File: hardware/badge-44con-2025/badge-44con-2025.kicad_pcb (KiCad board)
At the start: 2 copper layers, 100 x 100 mm, 28 parts, among them J1 128x64 OLED Display, J2 Conn_02x03_Odd_Even, SW1 RESET, SW2 SW_Nidec_CAS-120A1, U1 ESP32-WEMOS D1 mini, U2 CH32V003FxPx, U3 MT3608_Boost_converter, U4 AD8317_Module

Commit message: feat(Hw):Added_labels_and_changed_switch
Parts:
- added kibuzzard-68957673: G***, kibuzzard-68957673, B.Cu at (123.2, 124.5)
- added kibuzzard-689576B7: G***, kibuzzard-689576B7, B.Cu at (123.7, 107.6)
- added kibuzzard-689576CB: G***, kibuzzard-689576CB, B.Cu at (125.8, 48.4)
- added kibuzzard-689576F4: G***, kibuzzard-689576F4, B.Cu at (197.0, 68.4)
- added kibuzzard-689576FF: G***, kibuzzard-689576FF, B.Cu at (197.1, 70.5)
- added kibuzzard-68957745: G***, kibuzzard-68957745, B.Cu at (201.4, 77.7)
- added kibuzzard-6895776E: G***, kibuzzard-6895776E, B.Cu at (200.8, 78.6)
- added kibuzzard-68957B6E: G***, kibuzzard-68957B6E, B.Cu at (143.1, 132.1)
- added kibuzzard-68957F6B: G***, kibuzzard-68957F6B, B.Cu at (115.5, 118.0)
- JP2, JP3: footprint Jumper:SolderJumper-3_P1.3mm_Open_RoundedPad1.0x1.5mm -> Jumper:SolderJumper-3_P1.3mm_Bridged2Bar12_RoundedPad1.0x1.5mm
- SW2: footprint badge-44con-2025:a12013100ux0116 -> badge-44con-2025:JS102011SAQN; moved to B.Cu
- moved JP2 9.05 mm to (155.9, 63.0), turned to 0 degrees
- moved JP3 1.40 mm to (153.1, 55.7)
- moved SW2 1.07 mm to (110.8, 118.0)
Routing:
- net /CH3_SDA: track 22.2 -> 8.92 mm
- net /SDA_ESP: track 58.6 -> 54.1 mm, vias 1 -> 2
- net +5V: track 84.4 -> 88.2 mm, vias 0 -> 3
- net /CH3_SCL: track 19.2 -> 17.8 mm
- net /SCL: track 5.15 -> 3.89 mm
- net +5VP: track 77.1 -> 76.0 mm
- net /SCL_ESP: track 46.2 -> 45.2 mm
- net GND: vias 6 -> 33
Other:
- outline, holes or cut-outs redrawn

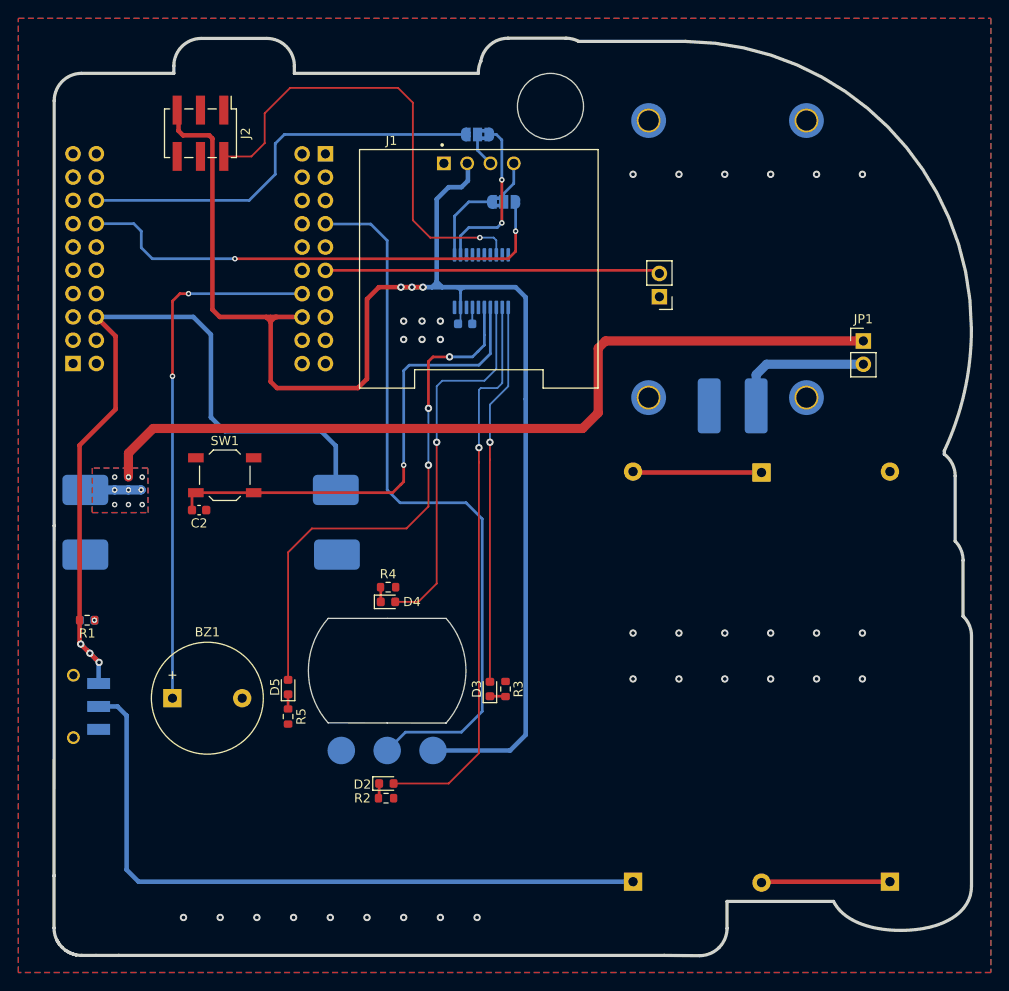
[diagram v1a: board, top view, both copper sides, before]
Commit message: feat(Hw):Added_buttons
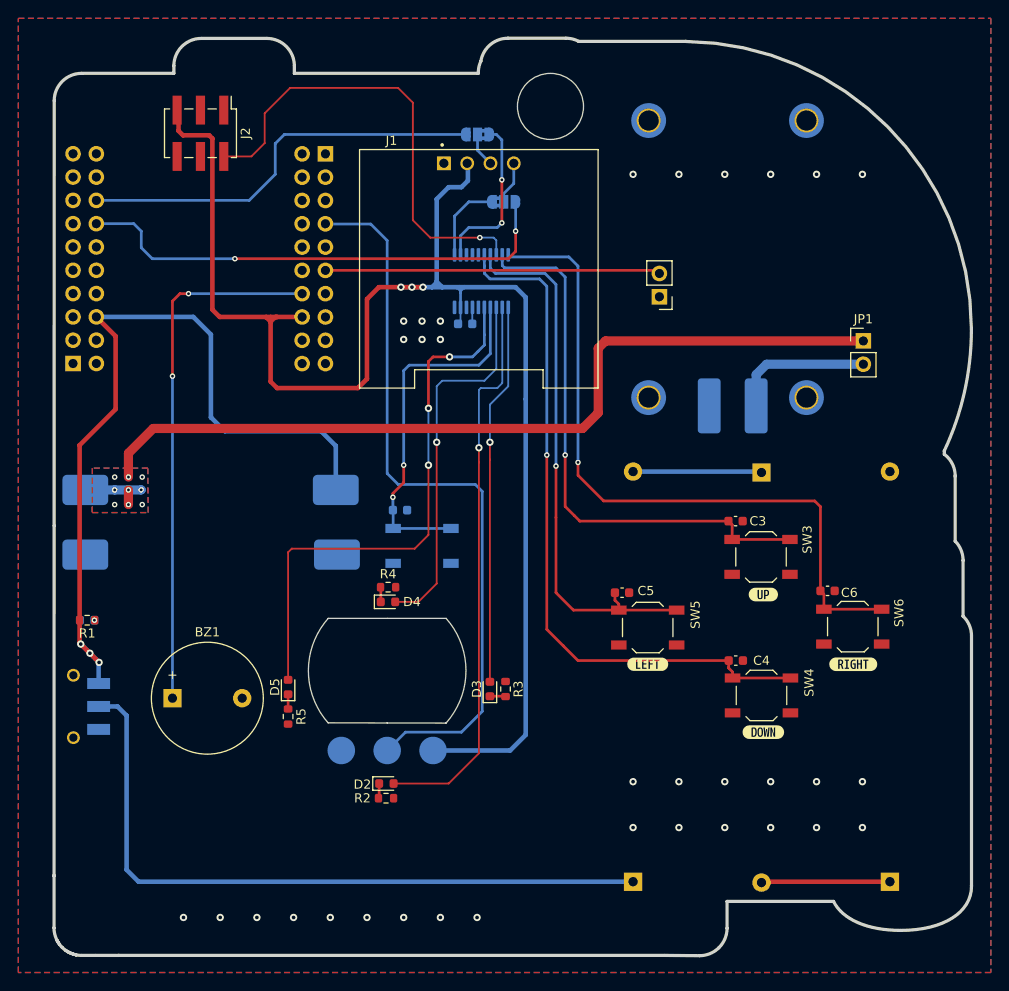
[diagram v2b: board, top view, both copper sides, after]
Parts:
- removed kibuzzard-68957745: G***, kibuzzard-68957745
- removed kibuzzard-6895776E: G***, kibuzzard-6895776E
- added C3: .1uF, Capacitor_SMD:C_0603_1608Metric, F.Cu at (181.2, 97.8)
- added C4: .1uF, Capacitor_SMD:C_0603_1608Metric, F.Cu at (181.2, 113.0)
- added C5: .1uF, Capacitor_SMD:C_0603_1608Metric, F.Cu at (168.8, 105.6)
- added C6: .1uF, Capacitor_SMD:C_0603_1608Metric, F.Cu at (191.2, 105.4)
- added SW3: UP, Button_Switch_SMD:SW_SPST_TL3342, F.Cu at (183.9, 101.7)
- added SW4: DOWN, Button_Switch_SMD:SW_SPST_TL3342, F.Cu at (184.0, 116.8)
- added SW5: LEFT, Button_Switch_SMD:SW_SPST_TL3342, F.Cu at (171.6, 109.4)
- added SW6: RIGHT, Button_Switch_SMD:SW_SPST_TL3342, F.Cu at (193.9, 109.3)
- added kibuzzard-689581B6: G***, kibuzzard-689581B6, B.Cu at (149.4, 96.6)
- added kibuzzard-68958540: G***, kibuzzard-68958540, B.Cu at (199.4, 85.0)
- added kibuzzard-6895857B: G***, kibuzzard-6895857B, B.Cu at (199.4, 83.6)
- added kibuzzard-689585C0: G***, kibuzzard-689585C0, F.Cu at (184.2, 120.8)
- added kibuzzard-689585CD: G***, kibuzzard-689585CD, F.Cu at (184.2, 105.8)
- added kibuzzard-689585DD: G***, kibuzzard-689585DD, F.Cu at (171.6, 113.4)
- added kibuzzard-689585EE: G***, kibuzzard-689585EE, F.Cu at (194.0, 113.4)
- C2, SW1: moved to B.Cu
- moved SW1 22.8 mm to (147.0, 100.5)
- moved C2 21.9 mm to (144.6, 96.6)
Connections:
- U2 pad 16: unconnected-(U2-PC6-Pad16) -> /DOWN
- U2 pad 17: unconnected-(U2-PC7-Pad17) -> /LEFT
- U2 pad 19: unconnected-(U2-PD2-Pad19) -> /UP
- U2 pad 20: unconnected-(U2-PD3-Pad20) -> /RIGHT
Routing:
- net /DOWN: track 0.00 -> 76.4 mm, vias 0 -> 1
- net /RIGHT: track 0.00 -> 76.4 mm, vias 0 -> 1
- net /UP: track 0.00 -> 60.5 mm, vias 0 -> 1
- net /LEFT: track 0.00 -> 59.0 mm, vias 0 -> 1
- net /RST: track 52.6 -> 39.3 mm, vias 1 -> 2
- net /LED4: track 58.0 -> 59.8 mm
- net +9V: track 98.0 -> 99.6 mm
- net /POT: track 79.4 -> 80.2 mm

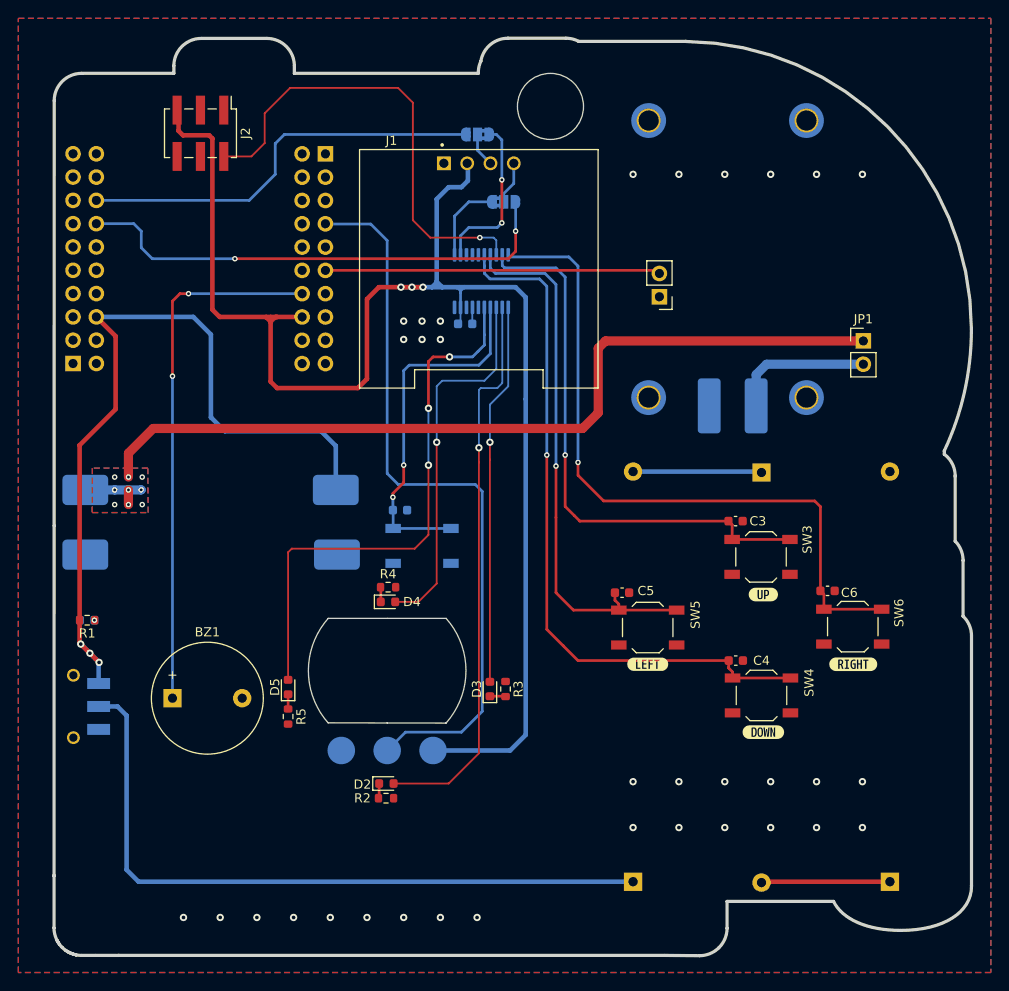
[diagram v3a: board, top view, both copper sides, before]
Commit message: feat(Hw):Footprints_replaced
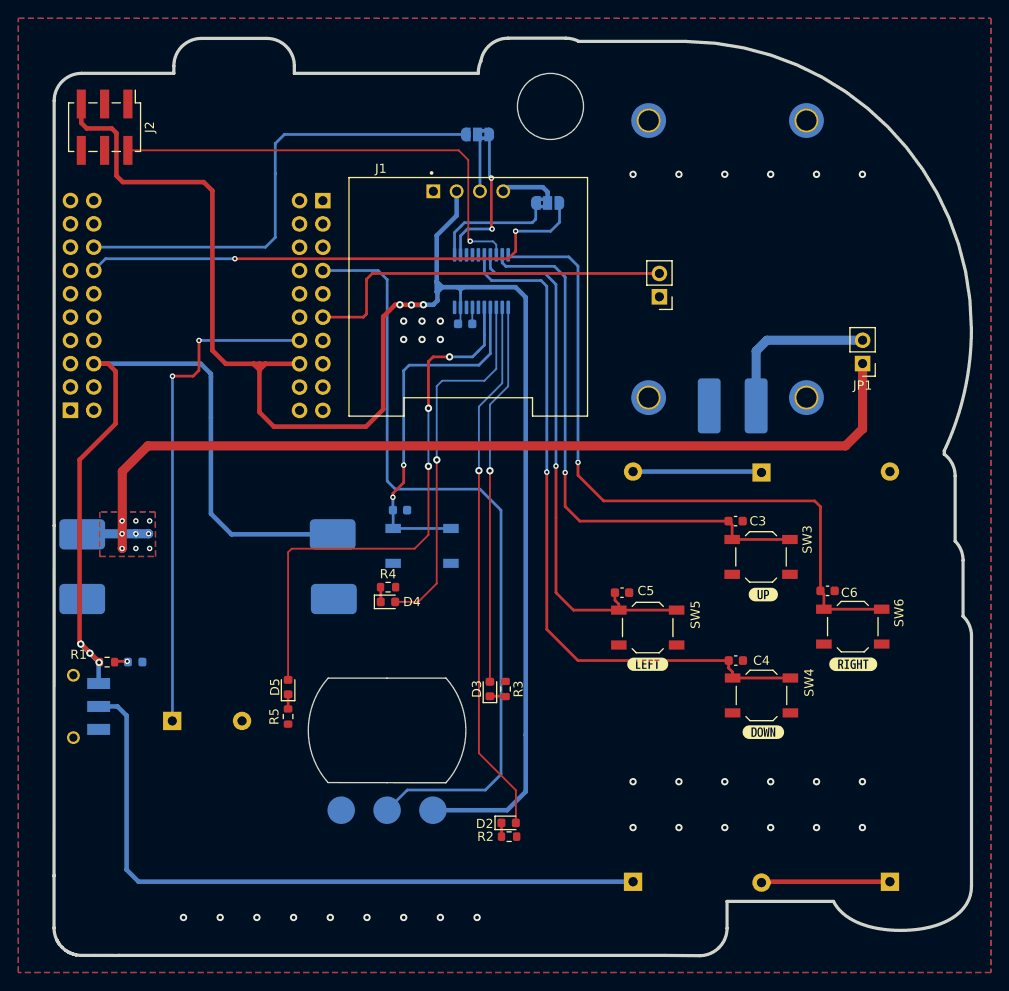
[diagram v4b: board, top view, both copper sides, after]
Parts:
- added G***: LOGO, badge-44con-2025:caution, B.Cu at (199.2, 69.1)
- BZ1: moved to B.Cu
- moved kibuzzard-689576CB 16.6 mm to (110.0, 53.3)
- moved R2 14.1 mm to (156.5, 132.2)
- moved D2 14.0 mm to (156.4, 130.7)
- moved J2 10.5 mm to (112.4, 54.9)
- moved kibuzzard-689576FF 9.81 mm to (196.9, 60.6)
- moved kibuzzard-689576F4 9.49 mm to (197.0, 58.9)
- moved kibuzzard-68958540 9.01 mm to (198.9, 76.0)
- moved kibuzzard-6895857B 8.77 mm to (199.0, 74.8)
- moved kibuzzard-689581B6 8.09 mm to (147.0, 104.3)
- moved D1 6.94 mm to (115.7, 113.2), turned to 180 degrees
- moved RV1 6.51 mm to (143.2, 120.6)
- moved kibuzzard-689576B7 5.76 mm to (127.2, 112.1)
- moved U1 5.11 mm to (137.9, 93.8)
- moved R1 5.06 mm to (112.7, 113.2)
- moved U3 4.85 mm to (140.0, 111.3)
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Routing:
- net +3.3V: track 165.7 -> 184.7 mm
- net /SCL_ESP: track 45.2 -> 51.6 mm
- net +9V: track 99.6 -> 105.4 mm
- net /POT: track 80.2 -> 85.9 mm
- net /CH3_SDA: track 8.92 -> 13.7 mm
- net /AD8317_OUT: track 36.5 -> 40.9 mm
- net +5V: track 88.2 -> 84.8 mm
- net /BUZZER: track 57.7 -> 55.0 mm
- net +9VA: track 15.6 -> 18.1 mm
- net /LED1: track 61.4 -> 58.9 mm
- net /SCL: track 3.89 -> 6.30 mm
- net /SDA_ESP: track 54.1 -> 56.3 mm
- net /SDA: track 4.66 -> 6.44 mm
- net /CH3_SCL: track 17.8 -> 16.2 mm
- net Net-(D1-A): track 0.00 -> 1.52 mm
